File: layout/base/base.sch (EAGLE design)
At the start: 29 parts, among them IC2 FT232RL, IC3 74ACT125D, P1 FSM4JSMA-SMD, T1 BC848, T2 BC848

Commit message: base schematic w/o IC3 but w/ all dev board holes
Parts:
- removed C1, C8: 100n, rcl:C-EUC0603
- removed C10: 22u, rcl-2:C-EUC0805
- removed IC3: 74ACT125D, 74xx-eu:74ACT125D
- removed JP1: USBA-SMD-MALE, SparkFun-Connectors:USBA-SMD-MALE
- removed JP2: (no value), pinhead-2:PINHD-2X04_2.54-SMD
- removed JP3, JP4: (no value), pinhead-2:PINHD-1X12_2.54
- removed R5, R6: 10k, rcl-2:R-EU_R0603
- added C11: 22u, rcl-2:C-EUC0805
- added JP5, JP6: (no value), pinhead-2:PINHD-2X12_2.54
- added SV1, SV2: (no value), sid:1X4SMD-2.54
- added U$1: USB-MALE-SMT, sid:USB-MALE-SMT
- C6: value 100n -> 22u; device rcl:C-EUC0603 -> rcl-2:C-EUC0805
- C7: value 100u 6,3V -> 22u; device cap-master:CP-7343-TE-D -> rcl-2:C-EUC0805
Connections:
- removed net N$10: IC3D.O, JP2.6
- removed net N$35: IC3A.O, JP2.3
- removed net N$36: IC3B.O, JP2.5
- removed net N$9: IC3C.O, JP2.4
- new net N$11: JP5.3, JP5.4
- new net N$13: JP5.5, JP5.6
- new net N$14: JP5.7, JP5.8
- new net N$15: JP5.10, JP5.9
- new net N$16: JP5.11, JP5.12
- new net N$17: JP5.13, JP5.14
- new net N$18: JP6.1, JP6.2
- new net N$19: JP6.5, JP6.6
- new net N$20: JP6.7, JP6.8
- new net N$21: JP6.10, JP6.9
- new net N$22: JP6.15, JP6.16
- new net N$23: JP6.17, JP6.18
- net +3V3: now also C11.1, JP5.21, JP5.22; no longer C7.+, JP3.11
- net +5V: now also C7.1, JP5.23, JP5.24, SV1.1, SV2.4; no longer C1.1, C10.1, C8.1, IC3P.VCC, JP2.1, JP2.8, JP4.1, R5.1, R6.2
- net CI: now also JP6.11, JP6.12, SV1.3, SV2.2; no longer IC3B.I, IC3C.I, JP4.7
- net DI: now also JP6.13, JP6.14, SV1.2, SV2.3; no longer IC3A.I, IC3D.I, JP4.6
- net GND: now also C11.2, C7.2, JP5.19, JP5.20, JP6.23, JP6.24, SV1.4, SV2.1, U$1.GND, U$1.S1, U$1.S2; no longer C1.2, C10.2, C7.-, C8.2, IC3P.GND, JP1.GND, JP2.2, JP2.7, JP3.10, JP3.12
- net GPIO0: now also JP6.19, JP6.20; no longer JP4.3
- net N$2: now also U$1.VBUS; no longer JP1.VBUS
- net N$3: now also U$1.D+; no longer JP1.D+
- net N$4: now also U$1.D-; no longer JP1.D-
- net RST: now also JP6.3, JP6.4; no longer JP4.11
- net RX: now also JP5.15, JP5.16; no longer JP3.8
- net SSL: now also JP6.21, JP6.22; no longer IC3A.OE, IC3B.OE, JP4.2, R5.2
- net SSR: now also JP5.1, JP5.2; no longer IC3C.OE, IC3D.OE, JP3.1, R6.1
- net TX: now also JP5.17, JP5.18; no longer JP3.9
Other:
- moved on the sheet: C2, C5, C6, IC1, IC2, P1, R3, R4, T1, T2

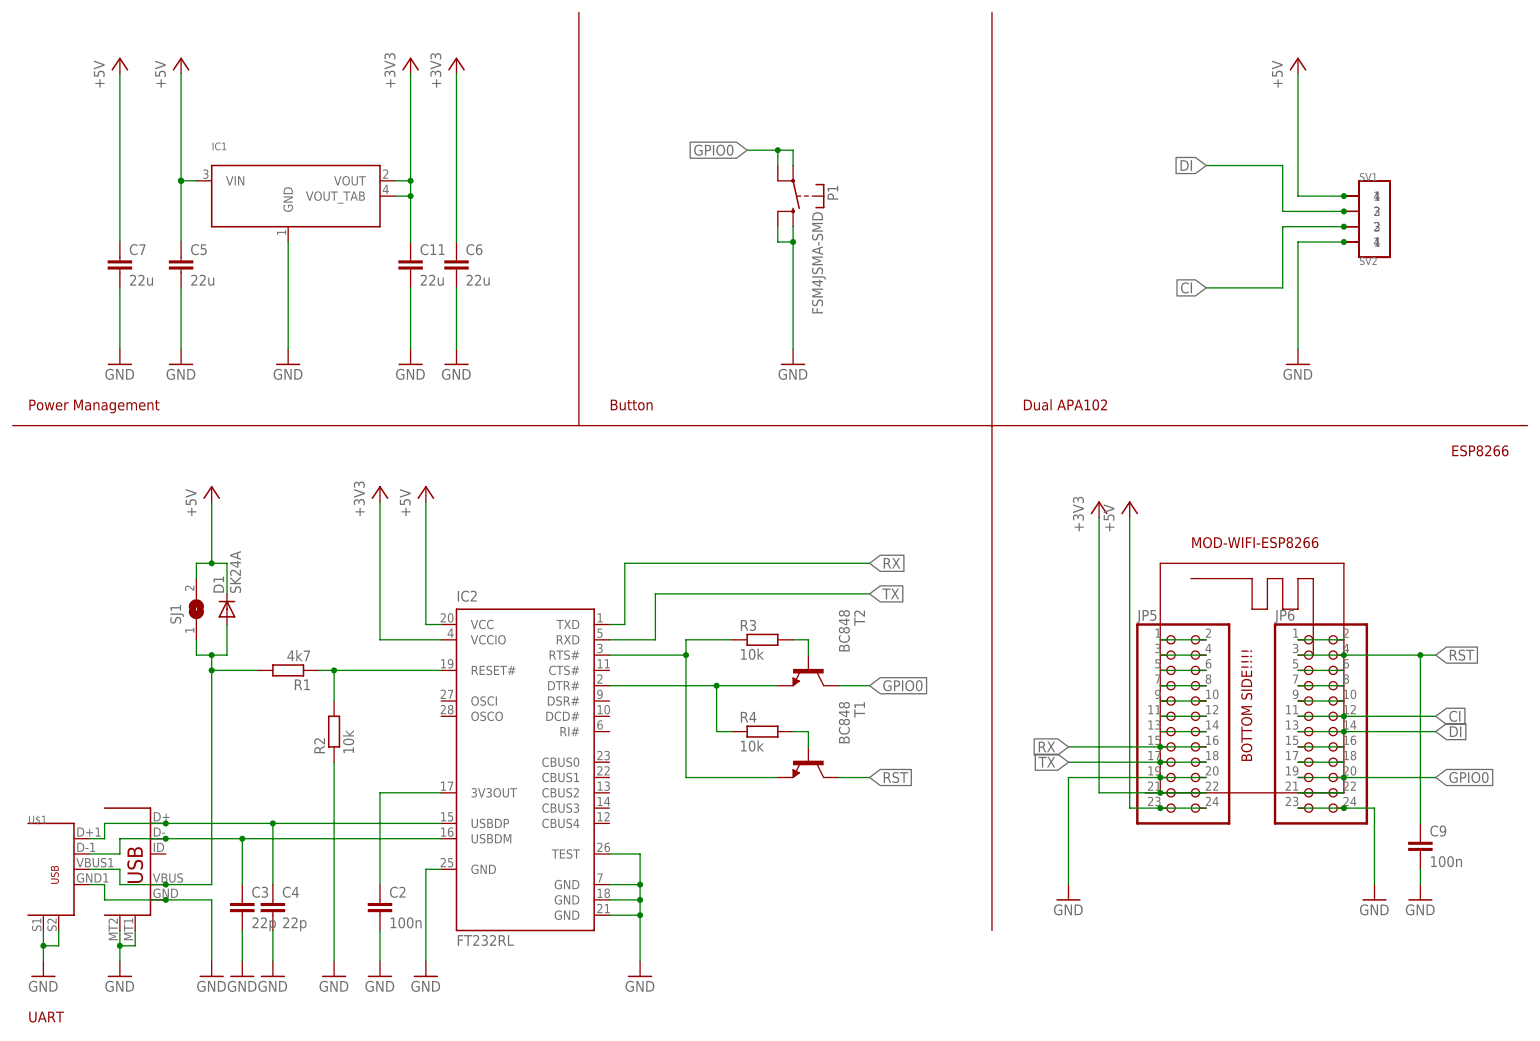
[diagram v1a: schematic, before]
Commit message: Bauteilbeschriftung der Platinen base und 4watt geordnet. Bestückungspläne hinzugefügt.
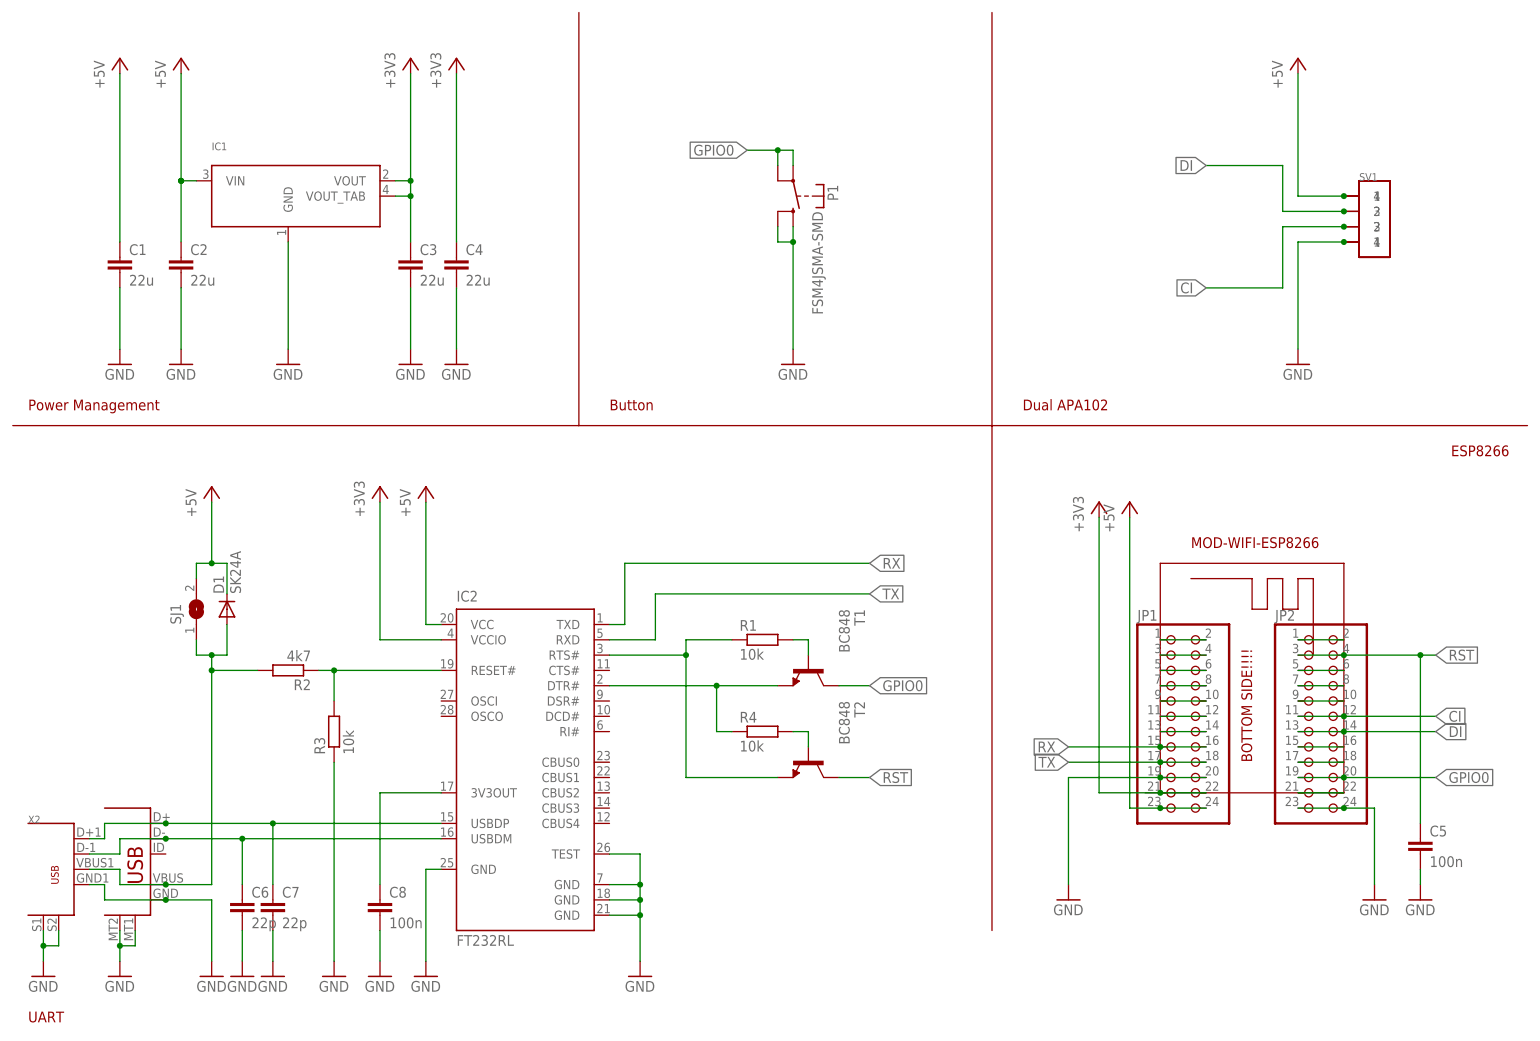
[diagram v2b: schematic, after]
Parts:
- removed C11: 22u, rcl-2:C-EUC0805
- removed C9: 100n, rcl:C-EUC0603
- added C1: 22u, rcl-2:C-EUC0805
- added C8: 100n, rcl:C-EUC0603
- C2: value 100n -> 22u; device rcl:C-EUC0603 -> rcl-2:C-EUC0805
- C3, C4: value 22p -> 22u; device rcl:C-EUC0603 -> rcl-2:C-EUC0805
- C5: value 22u -> 100n; device rcl-2:C-EUC0805 -> rcl:C-EUC0603
- C6, C7: value 22u -> 22p; device rcl-2:C-EUC0805 -> rcl:C-EUC0603
- R1: value 4k7 -> 10k
- R2: value 10k -> 4k7
- renumbered JP5 to JP1, JP6 to JP2, U$1 to X2, U$40 to X1
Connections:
- net +3V3: now also C3.1, C4.1; no longer C11.1, C6.1
- net +5V: now also C1.1, C2.1; no longer C5.1, C7.1
- net GND: now also C1.2, C8.2, R3.1; no longer C11.2, C9.2, R2.1
- net GPIO0: now also T1.C; no longer T2.C
- net N$1: now also R1.1, T2.E; no longer R3.1, T1.E
- net N$12: now also C8.1; no longer C2.1
- net N$2: now also R2.2; no longer R1.2
- net N$3: now also C7.1; no longer C4.1
- net N$4: now also C6.1; no longer C3.1
- net N$5: now also T1.E; no longer T2.E
- net N$6: now also R2.1, R3.2; no longer R1.1, R2.2
- net N$7: now also R1.2, T1.B; no longer R3.2, T2.B
- net N$8: now also T2.B; no longer T1.B
- net RST: now also C5.1, T2.C; no longer C9.1, T1.C
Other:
- moved on the sheet: C2, C3, C4, C5, C6, C7, R1, R2, R3, T1, T2
